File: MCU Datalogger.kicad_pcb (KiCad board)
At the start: 2 copper layers, 50 x 31.5 mm, 29 parts, among them J1 Conn_01x04_Pin, J2 Conn_01x04_Pin, J3 Conn_01x09, J4 Conn_02x03_Odd_Even, U1 24LC1025, U2 24LC1025, U3 DS1337S_T_R, U4 ATMEGA328P-AN, Y1 32.768 KHz, Y2 16 MHz

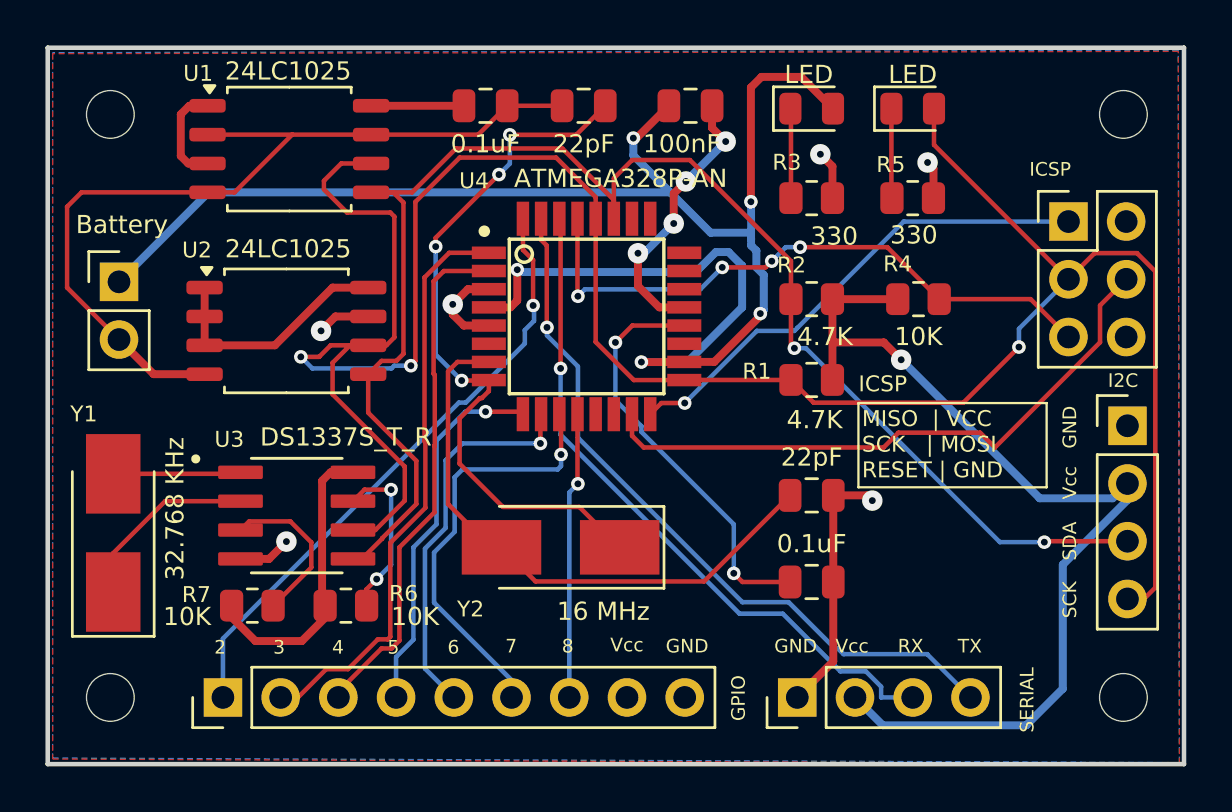
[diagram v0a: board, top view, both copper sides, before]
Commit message: fix pcb after the schematic bug
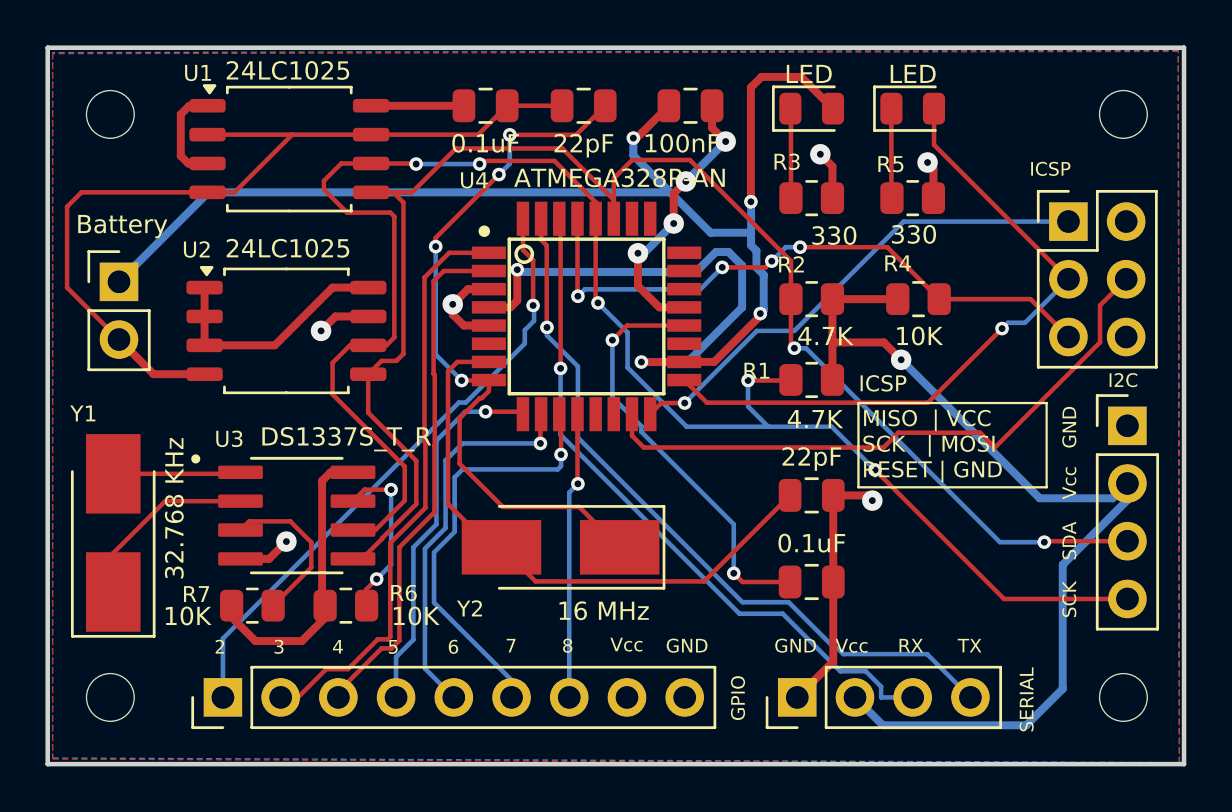
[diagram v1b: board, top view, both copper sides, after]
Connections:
- J1 pad 4: /SCK -> /SCL
- R1 pad 2: /SCK -> /SCL
- U1 pad 6: /SCK -> /SCL
- U2 pad 6: /SCK -> /SCL
- U3 pad 6: /SCK -> /SCL
- U4 pad 28: /SCK -> /SCL
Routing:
- net /SCK: track 111.2 -> 29.5 mm, vias 3 -> 1
- net /SCL: track 0.00 -> 74.1 mm, vias 0 -> 5
